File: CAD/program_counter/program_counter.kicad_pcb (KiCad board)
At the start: 2 copper layers, 100 x 50 mm, 56 parts, among them J1 Conn_01x18_Pin, J2 Conn_01x06_Pin, SW1 SW_Push, SW2 SW_Push, U1 74HC161, U2 74HC161, U3 74HC161, U4 74HC161, U5 74HC245, U6 74HC245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

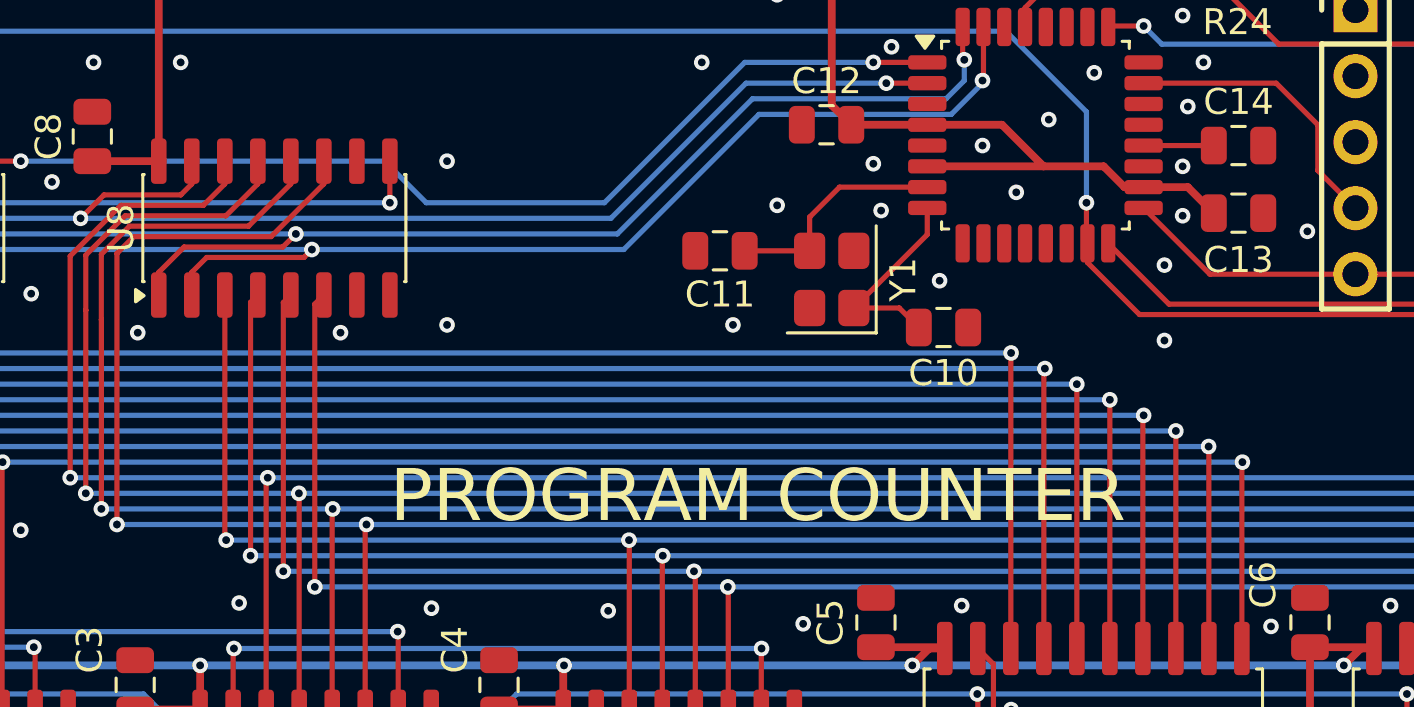
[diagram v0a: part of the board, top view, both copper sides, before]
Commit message: update PC, move crystal, change capacitors, add testpoints
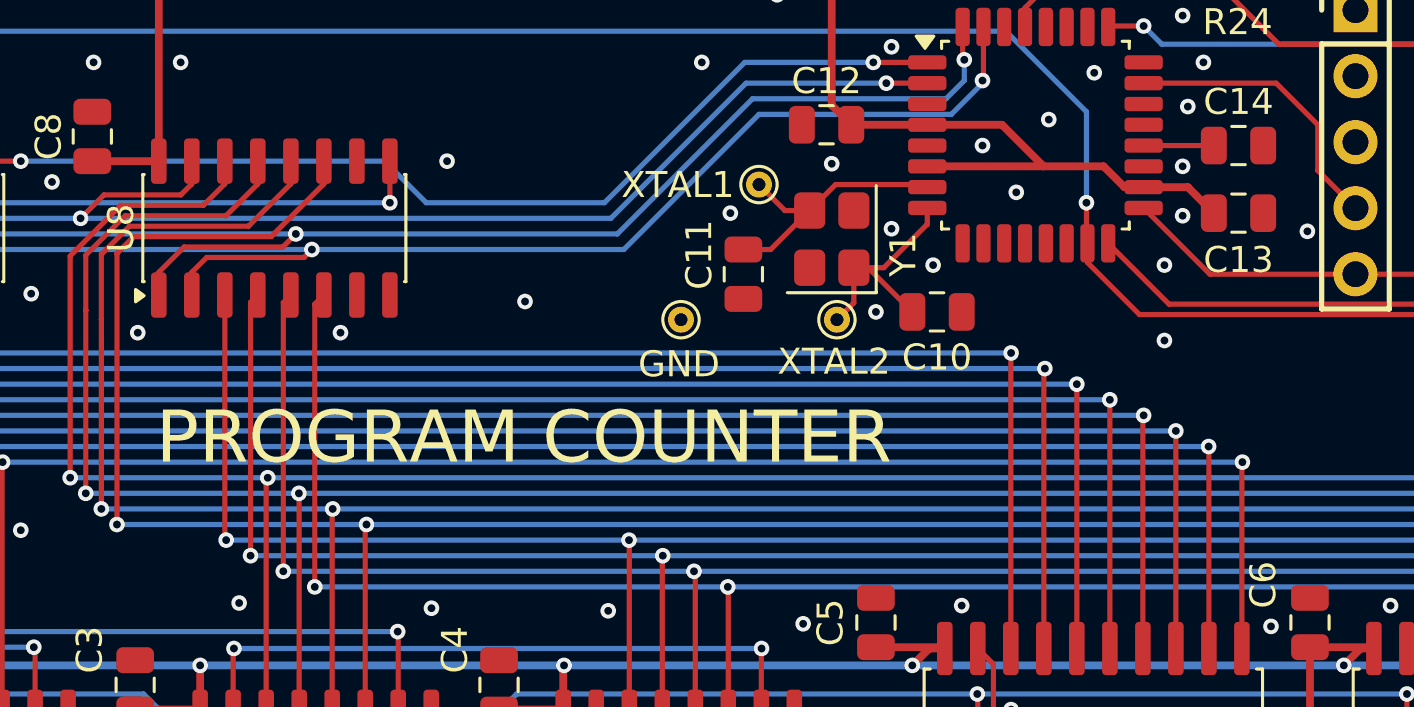
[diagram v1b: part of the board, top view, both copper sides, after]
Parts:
- added TP5: TestPoint, TestPoint:TestPoint_THTPad_D1.0mm_Drill0.5mm, F.Cu at (99.1, 63.2)
- added TP6: TestPoint, TestPoint:TestPoint_THTPad_D1.0mm_Drill0.5mm, F.Cu at (96.1, 58.0)
- added TP7: TestPoint, TestPoint:TestPoint_THTPad_D1.0mm_Drill0.5mm, F.Cu at (93.1, 63.2)
- C10, C11: value 22pF -> 12pF
- moved Y1 1.55 mm to (98.9, 60.1)
- moved C11 1.27 mm to (95.5, 61.5), turned to -90 degrees
- moved C10 0.65 mm to (103.0, 62.9)
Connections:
- net Net-(U9-XTAL1/PB6) renamed /xtal1
- net Net-(U9-XTAL2/PB7) renamed /xtal2
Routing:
- net /xtal1: track 8.80 -> 10.5 mm
- net /xtal2: track 7.83 -> 9.37 mm
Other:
- board text added: "XTAL1"
- board text added: "XTAL2"

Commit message: PC layout changes
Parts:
- moved C11 0.64 mm to (95.1, 61.0)

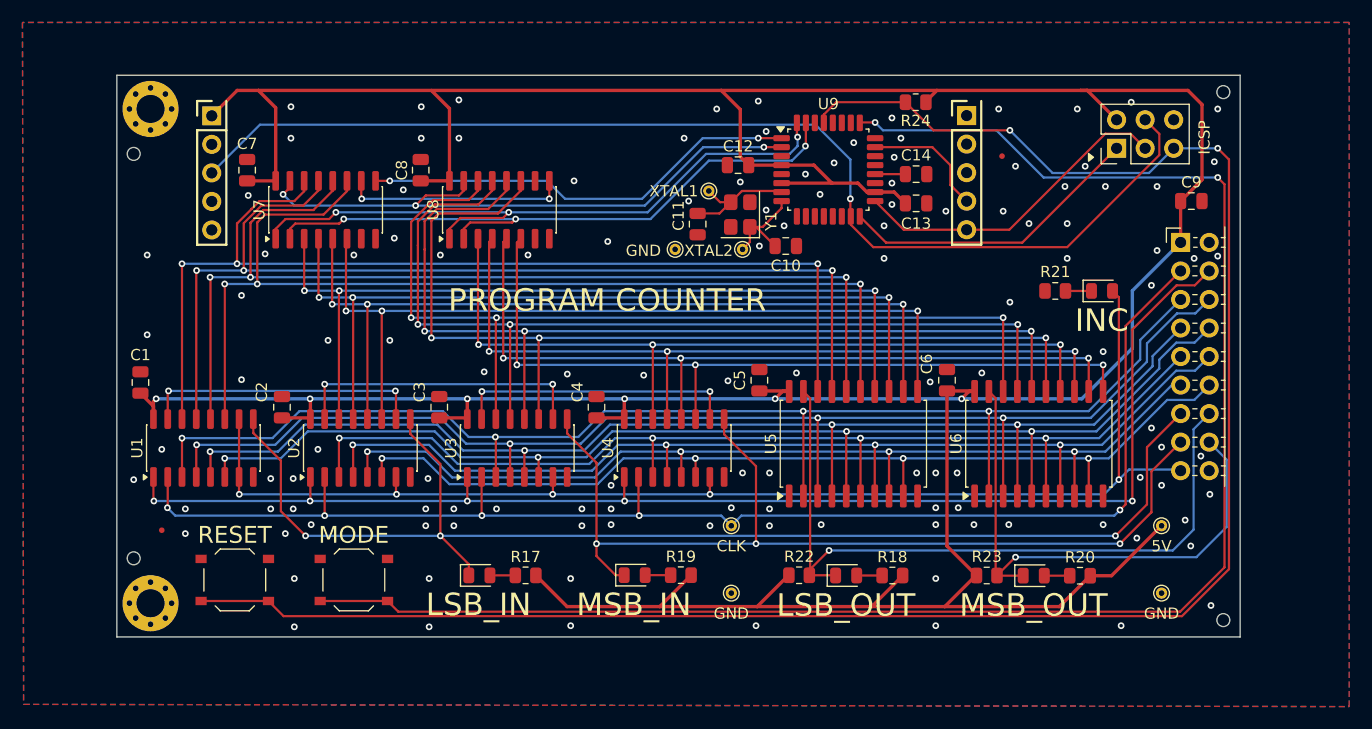
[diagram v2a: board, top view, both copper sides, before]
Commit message: layout improvements for program counter
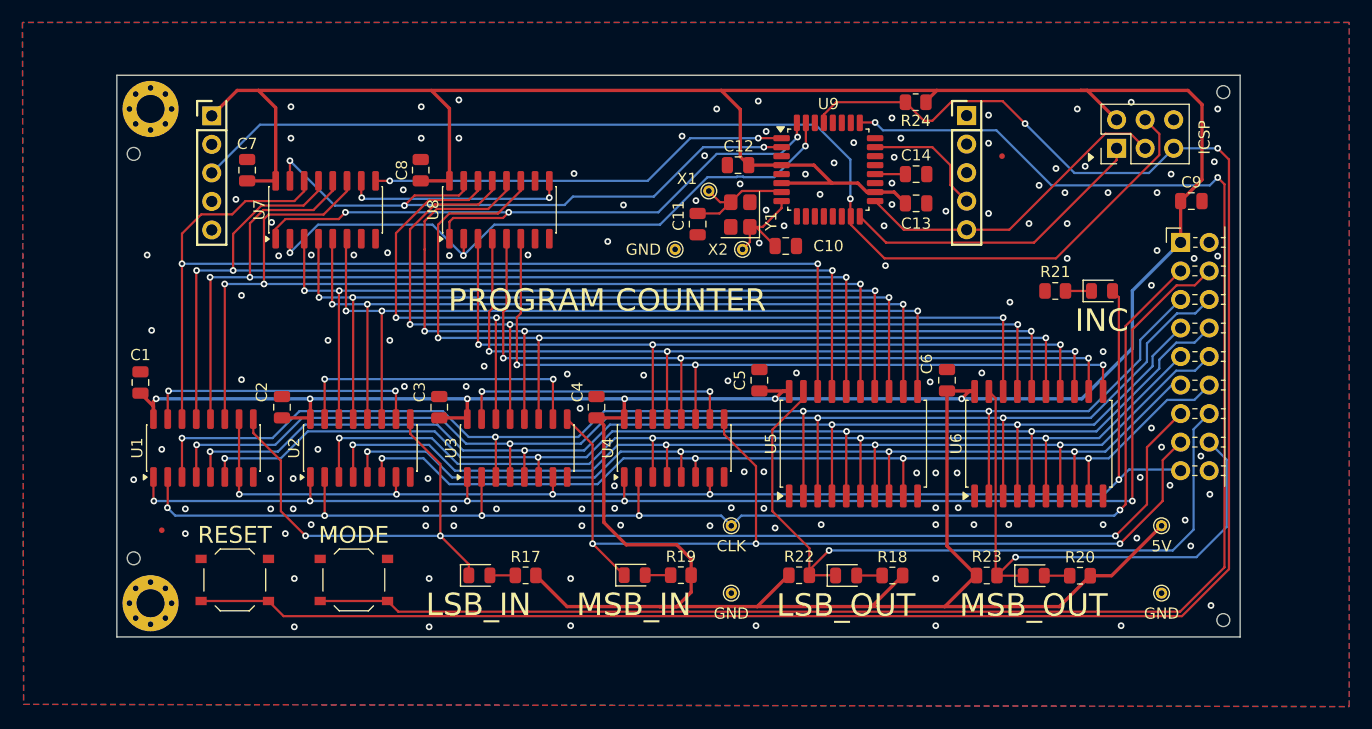
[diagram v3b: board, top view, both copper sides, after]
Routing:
- net +5V: track 377.4 -> 397.7 mm
- net /pc.0: track 93.5 -> 97.8 mm, vias 3 -> 2
- net /pc.8: track 84.8 -> 86.9 mm
- net ~{ce}: track 54.1 -> 56.1 mm
- net ~{RESET}: track 171.5 -> 172.9 mm
- net /pc.11: track 87.1 -> 85.7 mm
- net ser_in: track 39.0 -> 37.7 mm
- net ~{pc_L_out}: track 66.0 -> 67.2 mm
- net /pc.9: track 85.6 -> 86.6 mm
- net /rco.2-3: track 26.5 -> 27.5 mm
- net cp: track 57.8 -> 57.0 mm
- net MOSI: track 101.1 -> 101.9 mm
- net MISO: track 27.3 -> 27.9 mm
- net ~{sw_mode}: track 151.4 -> 151.9 mm
- net GND: vias 127 -> 137
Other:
- board text added: "X1"
- board text added: "X2"
- board text removed: "XTAL1"
- board text removed: "XTAL2"
